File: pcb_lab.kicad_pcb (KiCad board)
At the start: 4 copper layers, 118 x 250 mm, 277 parts, among them J12 SERVO, J201 XT60-M, J301 PI_GPIO_40, J302 CAN_A_PROBE, J303 CAN_B_PROBE, J501 Conn_01x03, J502 SWD, J504 Conn_01x06, J505 Conn_01x06, J506 CAN_A_PROBE, J507 CAN_B_PROBE, J508 Conn_01x13, J509 Conn_01x03, J510 SWD, Q201 AO4407A, SW11 219-2MSTR, SW12 219-2MSTR, SW13 CVS-01TB, SW14 CVS-01TB, SW301 219-2MSTR, SW302 219-2MSTR, SW303 CVS-01TB, SW304 CVS-01TB, SW501 SW_Push, SW502 219-2MSTR, SW503 219-2MSTR, SW504 CVS-01TB, SW505 CVS-01TB, SW506 SW_Push, U13 STM32F401RETx, U14 MCP2515T-I/ST, U15 MCP2515T-I/ST, U16 SN65HVD230DR, U17 SN65HVD230DR, U18 INA180A1IDBVT, U201 TPS564252DRLR, U202 TPS564252DRLR, U203 TPS564252DRLR, U301 MCP2515T-I/ST, U302 MCP2515T-I/ST, U303 SN65HVD230DR, U304 SN65HVD230DR, U501 STM32F401RETx, U502 L298P, U503 ACS712xLCTR-05B, U504 MCP2515T-I/ST, U505 MCP2515T-I/ST, U506 ACS712xLCTR-05B, U507 SN65HVD230DR, U508 SN65HVD230DR, Y301 16 MHz, Y302 16 MHz, Y5 16 MHz, Y501 16 MHz, Y502 16 MHz, Y6 16 MHz, Y7 16 MHz, Y8 16 MHz

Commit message: Reduced congestion on steering
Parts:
- moved TP201 113.4 mm to (115.5, 225.7), turned to 0 degrees
- moved R201 112.5 mm to (160.1, 184.8), turned to -90 degrees
- moved R202 112.4 mm to (158.3, 184.8), turned to 90 degrees
- moved C210 112.3 mm to (156.6, 184.8), turned to 90 degrees
- moved U201 110.4 mm to (154.4, 186.1), turned to 0 degrees
- moved R210 108.0 mm to (161.5, 188.1), turned to -90 degrees
- moved R207 107.8 mm to (157.5, 188.0), turned to -90 degrees
- moved C213 107.8 mm to (159.5, 188.1), turned to -90 degrees
- moved C207 107.5 mm to (154.7, 188.2), turned to 0 degrees
- moved L201 104.3 mm to (146.2, 190.9), turned to -90 degrees
- moved C204 103.9 mm to (154.9, 190.7), turned to 0 degrees
- moved C201 100.0 mm to (154.9, 193.5), turned to 0 degrees
- moved R213 98.2 mm to (159.6, 194.9), turned to -90 degrees
- moved C219 91.2 mm to (146.2, 200.3), turned to -90 degrees
- moved C222 90.9 mm to (148.9, 200.2), turned to -90 degrees
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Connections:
- R519 pad 1: /Steering/ST_ERR -> Net-(D516-A)
- R519 pad 2: Net-(D516-A) -> /Steering/ST_ERR
- U13 pad 26: unconnected-(U13-PB0-Pad26) -> /Steering/SERVO_PWM
- U13 pad 27: unconnected-(U13-PB1-Pad27) -> /Steering/ST_FR
- U13 pad 29: /Steering/ST_FL -> unconnected-(U13-PB10-Pad29)
- U13 pad 33: unconnected-(U13-PB12-Pad33) -> /Steering/ST_ERR
- U13 pad 34: /Steering/ST_CAN_TX_B -> /Steering/RELAY_TX
- U13 pad 35: /Steering/ST_CAN_TX_A -> /Steering/ST_FL
- U13 pad 36: /Steering/ST_CAN_RX_B -> unconnected-(U13-PB15-Pad36)
- U13 pad 37: /Steering/ST_CAN_RX_A -> unconnected-(U13-PC6-Pad37)
- U13 pad 41: /Steering/ST_FR -> /Steering/ST_CAN_TX_B
- U13 pad 42: /Steering/RELAY_TX -> /Steering/ST_CAN_TX_A
- U13 pad 44: unconnected-(U13-PA11-Pad44) -> /Steering/ST_CAN_RX_B
- U13 pad 45: unconnected-(U13-PA12-Pad45) -> /Steering/ST_CAN_RX_A
- U13 pad 53: /Steering/ST_ERR -> unconnected-(U13-PC12-Pad53)
- U13 pad 56: /Steering/SERVO_PWM -> unconnected-(U13-PB4-Pad56)
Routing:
- net GND: track 500.1 -> 1209.2 mm, vias 89 -> 94
- net (no net): track 689.9 -> 0.00 mm
- net 12V_BAT: track 176.6 -> 315.2 mm, vias 7 -> 8
- net 8V: track 28.5 -> 113.1 mm, vias 0 -> 3
- net /Steering/ST_SWDIO: track 31.5 -> 10.2 mm
- net /Steering/ST_ERR: track 55.8 -> 43.0 mm, vias 2 -> 0
- net /Steering/RELAY_TX: track 54.6 -> 42.1 mm
- net 3V3: track 175.6 -> 166.4 mm, vias 25 -> 26
- net /Steering/ST_CAN_TX_B: track 50.1 -> 40.9 mm, vias 2 -> 0
- net /Steering/ST_FR: track 118.7 -> 110.7 mm
- net /Steering/ST_CAN_B_CS: track 56.0 -> 48.6 mm
- net /Steering/ST_CAN_RX_A: track 50.8 -> 43.8 mm, vias 2 -> 0
- net /Steering/ST_FL: track 46.4 -> 40.3 mm, vias 2 -> 0
- net /Steering/ST_CAN_RX_B: track 48.2 -> 42.4 mm, vias 2 -> 0
- net /Steering/ST_CAN_TX_A: track 46.4 -> 41.7 mm, vias 2 -> 0
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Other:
- board text removed: "LED_YELLOW"
- board text removed: "ST_ERR"
- board text removed: "ST_FL"
- board text removed: "ST_FR"

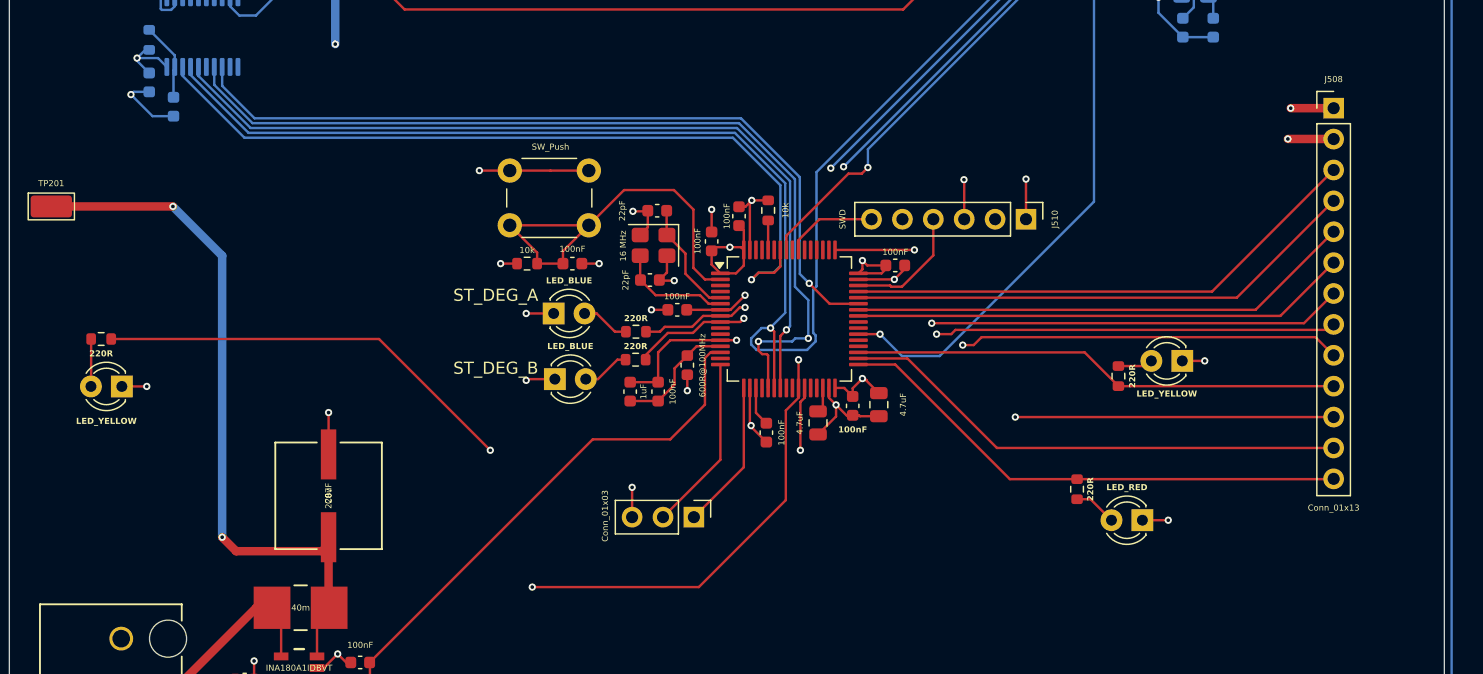
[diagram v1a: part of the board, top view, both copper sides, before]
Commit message: Replaced ST pin header with test points
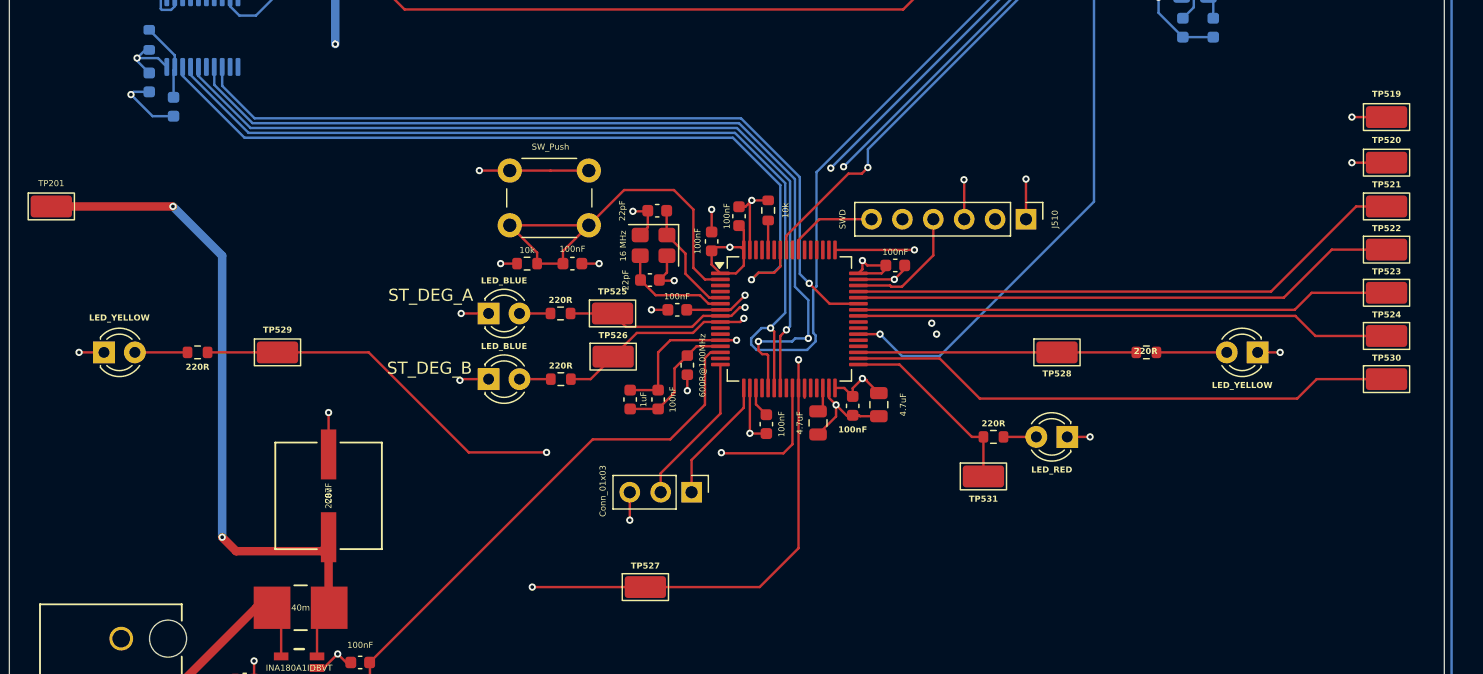
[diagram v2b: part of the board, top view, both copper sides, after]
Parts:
- removed J508: Conn_01x13, Connector_PinHeader_2.54mm:PinHeader_1x13_P2.54mm_Vertical
- added TP519: 5015, TestPoint:TestPoint_Keystone_5015_Micro_Mini, F.Cu at (225.2, 218.3)
- added TP520: 5015, TestPoint:TestPoint_Keystone_5015_Micro_Mini, F.Cu at (225.2, 222.1)
- added TP521: 5015, TestPoint:TestPoint_Keystone_5015_Micro_Mini, F.Cu at (225.2, 225.7)
- added TP522: 5015, TestPoint:TestPoint_Keystone_5015_Micro_Mini, F.Cu at (225.2, 229.2)
- added TP523: 5015, TestPoint:TestPoint_Keystone_5015_Micro_Mini, F.Cu at (225.2, 232.8)
- added TP524: 5015, TestPoint:TestPoint_Keystone_5015_Micro_Mini, F.Cu at (225.2, 236.3)
- added TP525: 5015, TestPoint:TestPoint_Keystone_5015_Micro_Mini, F.Cu at (161.6, 234.5)
- added TP526: 5015, TestPoint:TestPoint_Keystone_5015_Micro_Mini, F.Cu at (161.7, 238.1)
- added TP527: 5015, TestPoint:TestPoint_Keystone_5015_Micro_Mini, F.Cu at (164.3, 257.0)
- added TP528: 5015, TestPoint:TestPoint_Keystone_5015_Micro_Mini, F.Cu at (198.2, 237.7)
- added TP529: 5015, TestPoint:TestPoint_Keystone_5015_Micro_Mini, F.Cu at (134.1, 237.7)
- added TP530: 5015, TestPoint:TestPoint_Keystone_5015_Micro_Mini, F.Cu at (225.2, 239.9)
- added TP531: 5015, TestPoint:TestPoint_Keystone_5015_Micro_Mini, F.Cu at (192.1, 247.9)
- moved D516 9.23 mm to (199.0, 244.7)
- moved R519 8.11 mm to (192.9, 244.7), turned to 180 degrees
- moved R520 8.00 mm to (127.5, 237.7)
- moved R518 6.38 mm to (157.3, 234.5)
- moved R521 6.35 mm to (157.3, 239.9)
- moved D517 6.24 mm to (214.7, 237.7)
- moved D515 5.45 mm to (151.4, 239.9)
- moved D514 5.35 mm to (151.4, 234.5)
- moved D518 3.16 mm to (119.8, 237.7), turned to 0 degrees
- moved R522 3.02 mm to (205.5, 237.7), turned to 180 degrees
- moved J509 2.06 mm to (168.1, 249.2)
- moved C534 0.70 mm to (174.2, 243.6)
- moved C531 0.65 mm to (165.3, 241.6)
- moved C539 0.65 mm to (163.1, 241.6)
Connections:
- U13 pad 25: unconnected-(U13-PC5-Pad25) -> /Steering/ST_FR
- U13 pad 27: /Steering/ST_FR -> unconnected-(U13-PB1-Pad27)
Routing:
- net /Steering/ST_FR: track 110.7 -> 56.5 mm, vias 3 -> 2
- net /Steering/SERVO_PWM: track 116.8 -> 76.0 mm, vias 3 -> 2
- net /Steering/ST_DEG_A: track 58.9 -> 31.4 mm
- net /Steering/ST_ERR: track 43.0 -> 16.0 mm
- net /Steering/ST_DEG_B: track 59.1 -> 32.7 mm
- net /Steering/ST_FL: track 40.3 -> 22.9 mm
- net /Steering/RELAY_TX: track 42.1 -> 45.5 mm
- net /Steering/ST_CAN_TX_B: track 40.9 -> 44.1 mm
- net /Steering/ST_CAN_RX_B: track 42.4 -> 45.3 mm
- net Net-(D517-A): track 2.92 -> 5.79 mm
- net /Steering/ST_CAN_RX_A: track 43.8 -> 46.3 mm
- net /Steering/ST_CAN_TX_A: track 41.7 -> 44.0 mm
- net /Steering/ST_UART_RX: track 12.3 -> 10.4 mm
- net /Steering/ST_UART_TX: track 14.5 -> 12.5 mm
- net Net-(D514-A): track 4.02 -> 2.55 mm
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
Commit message: Congestion relief
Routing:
- net /Steering/ST_DEG_B: track 32.7 -> 14.2 mm, vias 2 -> 0
- net /Steering/ST_DEG_A: track 31.4 -> 13.1 mm, vias 2 -> 0
- net /Steering/SERVO_PWM: track 76.0 -> 72.0 mm, vias 2 -> 1
- net /Steering/ST_SPI_SCLK: track 116.5 -> 119.3 mm
- net /Steering/ST_SPI_MISO: track 123.5 -> 120.7 mm
- net GND: track 1207.8 -> 1207.0 mm

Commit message: All DRC errors clean
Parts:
- U201, U202, U203: footprint Package_TO_SOT_SMD:SOT-563 -> TPS564252DRLR:SOT6_DRL_TEX-M
- moved C512 17.3 mm to (161.2, 64.0), turned to 180 degrees
- moved D501 16.7 mm to (138.4, 91.7)
- moved D502 16.3 mm to (138.4, 96.8)
- moved J506 13.4 mm to (126.5, 159.9), turned to 90 degrees
- moved J302 12.8 mm to (129.2, 118.2)
- moved TP513 9.97 mm to (155.2, 109.0)
- moved TP514 9.96 mm to (155.2, 101.9)
- moved SW501 2.15 mm to (153.1, 93.0)
- moved C210 1.40 mm to (158.0, 184.7)
- moved R201 1.40 mm to (161.5, 184.7)
- moved R202 1.40 mm to (159.7, 184.7)
- moved U201 0.87 mm to (155.0, 185.5)
- moved U203 0.82 mm to (161.9, 42.8)
- moved R207 0.51 mm to (158.0, 188.1)
- moved C213 0.50 mm to (160.0, 188.1)
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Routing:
- net GND: track 1207.0 -> 545.5 mm, vias 94 -> 100
- net CANH_A: track 171.8 -> 130.3 mm, vias 5 -> 2
- net 5V: track 210.3 -> 237.3 mm, vias 3 -> 4
- net CANL_A: track 147.5 -> 123.4 mm, vias 5 -> 3
- net 12V_BAT: track 315.2 -> 336.7 mm, vias 8 -> 9
- net Net-(D501-A): track 2.59 -> 19.5 mm
- net Net-(D502-A): track 2.53 -> 18.0 mm
- net /Drivetrain/DT_DEG_A: track 28.3 -> 17.2 mm
- net /Drivetrain/DT_DEG_B: track 27.1 -> 17.6 mm
- net /Drivetrain/DT_SELF_TEST: track 31.5 -> 37.1 mm
- net /Cockpit/PI_SPI_MISO: track 169.4 -> 174.2 mm
- net /Cockpit/PI_CAN_B_CS: track 87.3 -> 91.8 mm
- net 3V3: track 165.7 -> 168.0 mm, vias 26 -> 27
- net /Cockpit/CAN_TX_B: track 103.9 -> 106.1 mm
- net Net-(U203-FB): track 9.56 -> 8.69 mm
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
